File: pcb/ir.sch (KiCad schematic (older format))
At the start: 2 parts, among them Q1 AO3400

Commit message: Fix Merges
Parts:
- Q1: symbol rasbot:AO3400 -> rasbot-rescue:AO3400-rasbot
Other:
- moved on the sheet: Q1
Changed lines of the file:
@@
 EESchema Schematic File Version 4
 LIBS:rasbot-cache
-LIBS:inter-cache
 EELAYER 29 0
 EELAYER END
@@
 IR_OUT6
 $Comp
-L power:GND #PWR0102
+L power:GND #PWR021
 U 1 1 5D41F6C3
 P 5300 7250
@@
 $EndSheet
 $Comp
-L rasbot:AO3400 Q1
+L rasbot-rescue:AO3400-rasbot Q1
 U 1 1 5D362773
 P 5250 6950
+AR Path="/5D362773" Ref="Q1"  Part="1"
+AR Path="/5D1373A3/5D25183D/5D362773" Ref="Q1"  Part="1"
 F 0 "Q1" H 5406 6996 50  0000 L CNN
 F 1 "AO3400" H 5406 6905 50  0000 L CNN

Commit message: Fix and Anotate design
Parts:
- removed Q1: AO3400, Package_TO_SOT_SMD:SOT-23, symbol rasbot-rescue:AO3400-rasbot
- added Q1: AO3400, Package_TO_SOT_SMD:SOT-23, symbol rasbot:AO3400
- gave numbers to parts that had none: 1
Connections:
- net GND: now also Q1.2 (S)
- net IR_Row0/v-: now also Q1.3 (D)
- net en: now also Q1.1 (G)
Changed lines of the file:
@@
 EESchema Schematic File Version 4
-LIBS:rasbot-cache
 EELAYER 29 0
 EELAYER END
@@
 IR_OUT6
 $Comp
-L power:GND #PWR021
+L power:GND #PWR020
 U 1 1 5D41F6C3
 P 5300 7250
-F 0 "#PWR021" H 5300 7000 50  0001 C CNN
+F 0 "#PWR020" H 5300 7000 50  0001 C CNN
 F 1 "GND" H 5305 7077 50  0000 C CNN
 F 2 "" H 5300 7250 50  0001 C CNN
@@
 F6 "OUT" I R 6250 2950 50
 $EndSheet
-$Comp
-L rasbot-rescue:AO3400-rasbot Q1
-U 1 1 5D362773
-P 5250 6950
-AR Path="/5D362773" Ref="Q1"  Part="1"
-AR Path="/5D1373A3/5D25183D/5D362773" Ref="Q1"  Part="1"
-F 0 "Q1" H 5406 6996 50  0000 L CNN
-F 1 "AO3400" H 5406 6905 50  0000 L CNN
-F 2 "Package_TO_SOT_SMD:SOT-23" H 5975 6875 50  0001 C CNN
-F 3 "http://dalincom.ru/datasheet/AO3400.pdf" H 5250 6950 50  0001 C CNN
-	1    5250 6950
-	1    0    0    -1
-$EndComp
 Wire Wire Line
 	5300 6750 5300 6700
 $Comp
-L Device:R R?
+L Device:R R4
 U 1 1 5D3ABC64
 P 5850 6950
-F 0 "R?" H 5920 6996 50  0000 L CNN
+F 0 "R4" H 5920 6996 50  0000 L CNN
 F 1 "0" H 5920 6905 50  0000 L CNN
 F 2 "" V 5780 6950 50  0001 C CNN
@@
 Wire Bus Line
 	4950 1000 4950 6150
+$Comp
+L rasbot:AO3400 Q1
+U 1 1 5D3E0C2F
+P 5150 6950
+F 0 "Q1" H 5406 6996 50  0000 L CNN
+F 1 "AO3400" H 5406 6905 50  0000 L CNN
+F 2 "Package_TO_SOT_SMD:SOT-23" H 5975 6875 50  0001 C CNN
+F 3 "http://www.aosmd.com/pdfs/datasheet/ao3400.pdf" H 5250 6950 50  0001 C CNN
+	1    5150 6950
+	1    0    0    -1
+$EndComp
 $EndSCHEMATC

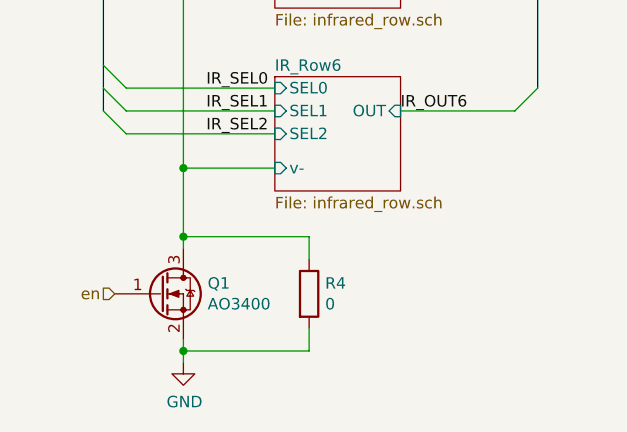
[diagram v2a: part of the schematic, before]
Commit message: MCU connections, OLED and Sonar
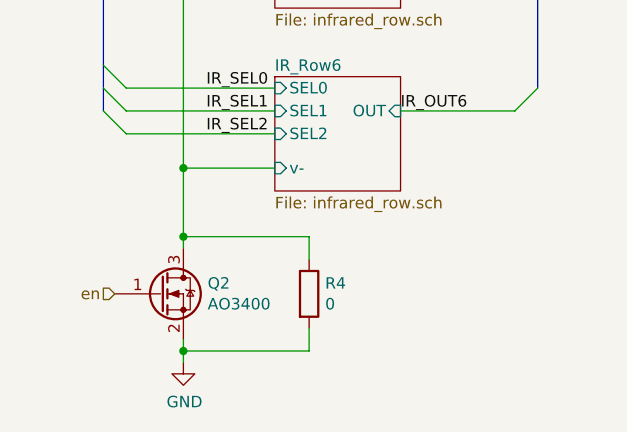
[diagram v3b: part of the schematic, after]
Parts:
- R4: footprint (none) -> Resistor_SMD:R_0805_2012Metric
- renumbered Q1 to Q2
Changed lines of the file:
@@
 IR_OUT6
 $Comp
-L power:GND #PWR020
+L power:GND #PWR031
 U 1 1 5D41F6C3
 P 5300 7250
-F 0 "#PWR020" H 5300 7000 50  0001 C CNN
+F 0 "#PWR031" H 5300 7000 50  0001 C CNN
 F 1 "GND" H 5305 7077 50  0000 C CNN
 F 2 "" H 5300 7250 50  0001 C CNN
@@
 F 0 "R4" H 5920 6996 50  0000 L CNN
 F 1 "0" H 5920 6905 50  0000 L CNN
-F 2 "" V 5780 6950 50  0001 C CNN
+F 2 "Resistor_SMD:R_0805_2012Metric" V 5780 6950 50  0001 C CNN
 F 3 "~" H 5850 6950 50  0001 C CNN
 	1    5850 6950
@@
 	4950 1000 4950 6150
 $Comp
-L rasbot:AO3400 Q1
+L rasbot:AO3400 Q2
 U 1 1 5D3E0C2F
 P 5150 6950
-F 0 "Q1" H 5406 6996 50  0000 L CNN
+F 0 "Q2" H 5406 6996 50  0000 L CNN
 F 1 "AO3400" H 5406 6905 50  0000 L CNN
 F 2 "Package_TO_SOT_SMD:SOT-23" H 5975 6875 50  0001 C CNN
